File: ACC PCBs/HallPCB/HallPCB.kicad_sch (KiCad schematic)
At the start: 2 parts, among them J1 Conn_01x04_Socket, U1 TLE49643MXTMA1

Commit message: All boards should be finished. ACC otw, and an earlier version of the main board otw
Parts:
- added U2: AP2127N-1.0, Package_TO_SOT_SMD:SOT-23, symbol Regulator_Linear:AP2127N-1.0
- J1: footprint (none) -> Connector_PinHeader_2.54mm:PinHeader_1x04_P2.54mm_Horizontal
- U1: footprint PG-SOT23-3-15_INF -> TLE49643MXTMA1:PG-SOT23-3-15_INF
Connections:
- net MAIN: now also U2.2 (VO)
- net RAWSWPOWER: now also U2.3 (VI)
- net VOUT: now also U1.2 (Q); no longer U1.1 (VDD)
- new net SIG: U1.1 (VDD), U2.1 (GATE)
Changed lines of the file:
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@@
 	(global_label "VOUT"
 		(shape input)
+		(at 160.02 107.95 0)
+		(fields_autoplaced yes)
+		(effects
+			(font
+				(size 1.27 1.27)
+			)
+			(justify left)
+		)
+		(property "Intersheetrefs" "${INTERSHEET_REFS}"
+			(at 167.7224 107.95 0)
+			(effects
+				(font
+					(size 1.27 1.27)
+				)
+				(justify left)
+				(hide yes)
+			)
+		)
+	)
+	(global_label "RAWSWPOWER"
+		(shape input)
+		(at 142.24 86.36 180)
+		(fields_autoplaced yes)
+		(effects
+			(font
+				(size 1.27 1.27)
+			)
+			(justify right)
+		)
+		(property "Intersheetrefs" "${INTERSHEET_REFS}"
+			(at 126.313 86.36 0)
+			(effects
+				(font
+					(size 1.27 1.27)
+				)
+				(justify right)
+				(hide yes)
+			)
+		)
+	)
+	(global_label "MAIN"
+		(shape input)
+		(at 149.86 121.92 0)
+		(fields_autoplaced yes)
+		(effects
+			(font
+				(size 1.27 1.27)
+			)
+			(justify left)
+		)
+		(property "Intersheetrefs" "${INTERSHEET_REFS}"
+			(at 157.3205 121.92 0)
+			(effects
+				(font
+					(size 1.27 1.27)
+				)
+				(justify left)
+				(hide yes)
+			)
+		)
+	)
+	(global_label "RAWSWPOWER"
+		(shape input)
+		(at 134.62 121.92 180)
+		(fields_autoplaced yes)
+		(effects
+			(font
+				(size 1.27 1.27)
+			)
+			(justify right)
+		)
+		(property "Intersheetrefs" "${INTERSHEET_REFS}"
+			(at 118.693 121.92 0)
+			(effects
+				(font
+					(size 1.27 1.27)
+				)
+				(justify right)
+				(hide yes)
+			)
+		)
+	)
+	(global_label "MAIN"
+		(shape input)
+		(at 142.24 81.28 180)
+		(fields_autoplaced yes)
+		(effects
+			(font
+				(size 1.27 1.27)
+			)
+			(justify right)
+		)
+		(property "Intersheetrefs" "${INTERSHEET_REFS}"
+			(at 134.7795 81.28 0)
+			(effects
+				(font
+					(size 1.27 1.27)
+				)
+				(justify right)
+				(hide yes)
+			)
+		)
+	)
+	(global_label "VOUT"
+		(shape input)
+		(at 142.24 88.9 180)
+		(fields_autoplaced yes)
+		(effects
+			(font
+				(size 1.27 1.27)
+			)
+			(justify right)
+		)
+		(property "Intersheetrefs" "${INTERSHEET_REFS}"
+			(at 134.5376 88.9 0)
+			(effects
+				(font
+					(size 1.27 1.27)
+				)
+				(justify right)
+				(hide yes)
+			)
+		)
+	)
+	(global_label "GND"
+		(shape input)
+		(at 142.24 83.82 180)
+		(fields_autoplaced yes)
+		(effects
+			(font
+				(size 1.27 1.27)
+			)
+			(justify right)
+		)
+		(property "Intersheetrefs" "${INTERSHEET_REFS}"
+			(at 135.3843 83.82 0)
+			(effects
+				(font
+					(size 1.27 1.27)
+				)
+				(justify right)
+				(hide yes)
+			)
+		)
+	)
+	(global_label "GND"
+		(shape input)
+		(at 160.02 105.41 0)
+		(fields_autoplaced yes)
+		(effects
+			(font
+				(size 1.27 1.27)
+			)
+			(justify left)
+		)
+		(property "Intersheetrefs" "${INTERSHEET_REFS}"
+			(at 166.8757 105.41 0)
+			(effects
+				(font
+					(size 1.27 1.27)
+				)
+				(justify left)
+				(hide yes)
+			)
+		)
+	)
+	(global_label "SIG"
+		(shape input)
+		(at 142.24 129.54 270)
+		(fields_autoplaced yes)
+		(effects
+			(font
+				(size 1.27 1.27)
+			)
+			(justify right)
+		)
+		(property "Intersheetrefs" "${INTERSHEET_REFS}"
+			(at 142.24 135.6095 90)
+			(effects
+				(font
+					(size 1.27 1.27)
+				)
+				(justify right)
+				(hide yes)
+			)
+		)
+	)
+	(global_label "SIG"
+		(shape input)
 		(at 119.38 105.41 180)
 		(fields_autoplaced yes)
@@
 		)
 		(property "Intersheetrefs" "${INTERSHEET_REFS}"
-			(at 111.6776 105.41 0)
-			(effects
-				(font
-					(size 1.27 1.27)
-				)
-				(justify right)
-				(hide yes)
-			)
-		)
-	)
-	(global_label "RAWSWPOWER"
-		(shape input)
-		(at 142.24 86.36 180)
-		(fields_autoplaced yes)
-		(effects
-			(font
-				(size 1.27 1.27)
-			)
-			(justify right)
-		)
-		(property "Intersheetrefs" "${INTERSHEET_REFS}"
-			(at 126.313 86.36 0)
-			(effects
-				(font
-					(size 1.27 1.27)
-				)
-				(justify right)
-				(hide yes)
-			)
-		)
-	)
-	(global_label "MAIN"
-		(shape input)
-		(at 142.24 81.28 180)
-		(fields_autoplaced yes)
-		(effects
-			(font
-				(size 1.27 1.27)
-			)
-			(justify right)
-		)
-		(property "Intersheetrefs" "${INTERSHEET_REFS}"
-			(at 134.7795 81.28 0)
-			(effects
-				(font
-					(size 1.27 1.27)
-				)
-				(justify right)
-				(hide yes)
-			)
-		)
-	)
-	(global_label "VOUT"
-		(shape input)
-		(at 142.24 88.9 180)
-		(fields_autoplaced yes)
-		(effects
-			(font
-				(size 1.27 1.27)
-			)
-			(justify right)
-		)
-		(property "Intersheetrefs" "${INTERSHEET_REFS}"
-			(at 134.5376 88.9 0)
-			(effects
-				(font
-					(size 1.27 1.27)
-				)
-				(justify right)
-				(hide yes)
-			)
-		)
-	)
-	(global_label "GND"
-		(shape input)
-		(at 142.24 83.82 180)
-		(fields_autoplaced yes)
-		(effects
-			(font
-				(size 1.27 1.27)
-			)
-			(justify right)
-		)
-		(property "Intersheetrefs" "${INTERSHEET_REFS}"
-			(at 135.3843 83.82 0)
-			(effects
-				(font
-					(size 1.27 1.27)
-				)
-				(justify right)
-				(hide yes)
-			)
-		)
-	)
-	(global_label "GND"
-		(shape input)
-		(at 160.02 105.41 0)
-		(fields_autoplaced yes)
-		(effects
-			(font
-				(size 1.27 1.27)
-			)
-			(justify left)
-		)
-		(property "Intersheetrefs" "${INTERSHEET_REFS}"
-			(at 166.8757 105.41 0)
-			(effects
-				(font
-					(size 1.27 1.27)
-				)
-				(justify left)
-				(hide yes)
+			(at 113.3105 105.41 0)
+			(effects
+				(font
+					(size 1.27 1.27)
+				)
+				(justify right)
+				(hide yes)
+			)
+		)
+	)
+	(symbol
+		(lib_id "Regulator_Linear:AP2127N-1.0")
+		(at 142.24 121.92 0)
+		(unit 1)
+		(exclude_from_sim no)
+		(in_bom yes)
+		(on_board yes)
+		(dnp no)
+		(fields_autoplaced yes)
+		(property "Reference" "U2"
+			(at 142.24 115.57 0)
+			(effects
+				(font
+					(size 1.27 1.27)
+				)
+			)
+		)
+		(property "Value" "AP2127N-1.0"
+			(at 142.24 118.11 0)
+			(effects
+				(font
+					(size 1.27 1.27)
+				)
+			)
+		)
+		(property "Footprint" "Package_TO_SOT_SMD:SOT-23"
+			(at 142.24 116.205 0)
+			(effects
+				(font
+					(size 1.27 1.27)
+					(italic yes)
+				)
+				(hide yes)
+			)
+		)
+		(property "Datasheet" "https://www.diodes.com/assets/Datasheets/AP2127.pdf"
+			(at 142.24 121.92 0)
+			(effects
+				(font
+					(size 1.27 1.27)
+				)
+				(hide yes)
+			)
+		)
+		(property "Description" "300mA low dropout linear regulator, shutdown pin, 2.5V-6V input voltage, 1.0V fixed positive output, SOT-23 package"
+			(at 142.24 121.92 0)
+			(effects
+				(font
+					(size 1.27 1.27)
+				)
+				(hide yes)
+			)
+		)
+		(pin "3"
+		)
+		(pin "1"
+		)
+		(pin "2"
+		)
+		(instances
+			(project ""
+				(path "/bca63e1f-d422-43ee-b63a-c2b8269ab195"
+					(reference "U2")
+					(unit 1)
+				)
 			)
 		)
@@
 			)
 		)
-		(property "Footprint" "PG-SOT23-3-15_INF"
+		(property "Footprint" "TLE49643MXTMA1:PG-SOT23-3-15_INF"
 			(at 119.38 105.41 0)
 			(effects
@@
 			)
 		)
-		(property "Footprint" ""
+		(property "Footprint" "Connector_PinHeader_2.54mm:PinHeader_1x04_P2.54mm_Horizontal"
 			(at 147.32 83.82 0)
 			(effects

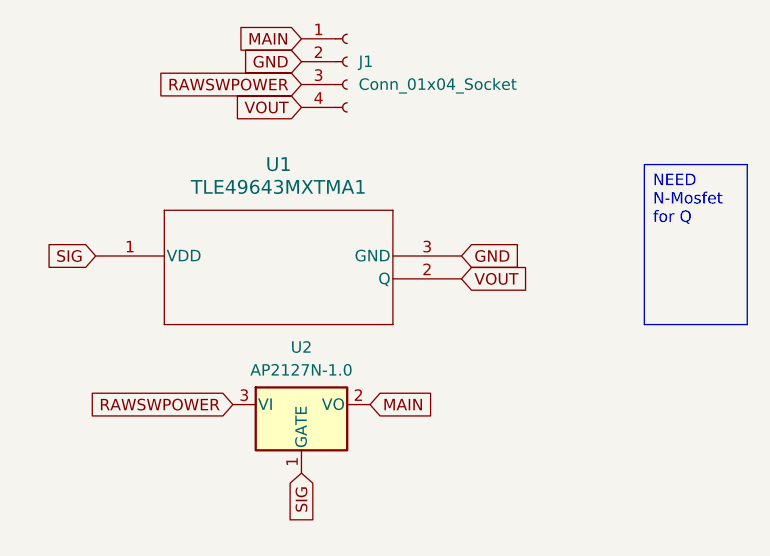
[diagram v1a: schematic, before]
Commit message: post R1 - flipped many traces and worked on adding an internal sensor for reduncancy
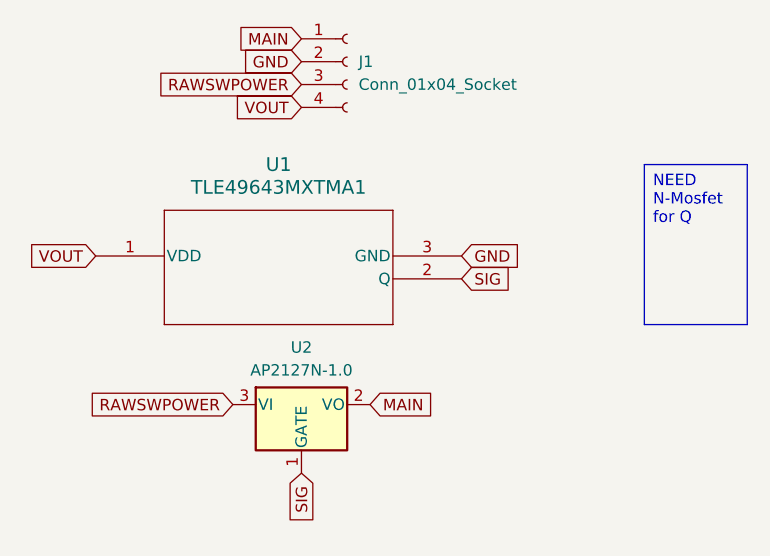
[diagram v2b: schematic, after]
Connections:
- net SIG: now also U1.2 (Q); no longer U1.1 (VDD)
- net VOUT: now also U1.1 (VDD); no longer U1.2 (Q)
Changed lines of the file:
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@@
 	(global_label "VOUT"
 		(shape input)
+		(at 119.38 105.41 180)
+		(fields_autoplaced yes)
+		(effects
+			(font
+				(size 1.27 1.27)
+			)
+			(justify right)
+		)
+		(property "Intersheetrefs" "${INTERSHEET_REFS}"
+			(at 111.6776 105.41 0)
+			(effects
+				(font
+					(size 1.27 1.27)
+				)
+				(justify right)
+				(hide yes)
+			)
+		)
+	)
+	(global_label "RAWSWPOWER"
+		(shape input)
+		(at 142.24 86.36 180)
+		(fields_autoplaced yes)
+		(effects
+			(font
+				(size 1.27 1.27)
+			)
+			(justify right)
+		)
+		(property "Intersheetrefs" "${INTERSHEET_REFS}"
+			(at 126.313 86.36 0)
+			(effects
+				(font
+					(size 1.27 1.27)
+				)
+				(justify right)
+				(hide yes)
+			)
+		)
+	)
+	(global_label "MAIN"
+		(shape input)
+		(at 149.86 121.92 0)
+		(fields_autoplaced yes)
+		(effects
+			(font
+				(size 1.27 1.27)
+			)
+			(justify left)
+		)
+		(property "Intersheetrefs" "${INTERSHEET_REFS}"
+			(at 157.3205 121.92 0)
+			(effects
+				(font
+					(size 1.27 1.27)
+				)
+				(justify left)
+				(hide yes)
+			)
+		)
+	)
+	(global_label "RAWSWPOWER"
+		(shape input)
+		(at 134.62 121.92 180)
+		(fields_autoplaced yes)
+		(effects
+			(font
+				(size 1.27 1.27)
+			)
+			(justify right)
+		)
+		(property "Intersheetrefs" "${INTERSHEET_REFS}"
+			(at 118.693 121.92 0)
+			(effects
+				(font
+					(size 1.27 1.27)
+				)
+				(justify right)
+				(hide yes)
+			)
+		)
+	)
+	(global_label "MAIN"
+		(shape input)
+		(at 142.24 81.28 180)
+		(fields_autoplaced yes)
+		(effects
+			(font
+				(size 1.27 1.27)
+			)
+			(justify right)
+		)
+		(property "Intersheetrefs" "${INTERSHEET_REFS}"
+			(at 134.7795 81.28 0)
+			(effects
+				(font
+					(size 1.27 1.27)
+				)
+				(justify right)
+				(hide yes)
+			)
+		)
+	)
+	(global_label "VOUT"
+		(shape input)
+		(at 142.24 88.9 180)
+		(fields_autoplaced yes)
+		(effects
+			(font
+				(size 1.27 1.27)
+			)
+			(justify right)
+		)
+		(property "Intersheetrefs" "${INTERSHEET_REFS}"
+			(at 134.5376 88.9 0)
+			(effects
+				(font
+					(size 1.27 1.27)
+				)
+				(justify right)
+				(hide yes)
+			)
+		)
+	)
+	(global_label "GND"
+		(shape input)
+		(at 142.24 83.82 180)
+		(fields_autoplaced yes)
+		(effects
+			(font
+				(size 1.27 1.27)
+			)
+			(justify right)
+		)
+		(property "Intersheetrefs" "${INTERSHEET_REFS}"
+			(at 135.3843 83.82 0)
+			(effects
+				(font
+					(size 1.27 1.27)
+				)
+				(justify right)
+				(hide yes)
+			)
+		)
+	)
+	(global_label "GND"
+		(shape input)
+		(at 160.02 105.41 0)
+		(fields_autoplaced yes)
+		(effects
+			(font
+				(size 1.27 1.27)
+			)
+			(justify left)
+		)
+		(property "Intersheetrefs" "${INTERSHEET_REFS}"
+			(at 166.8757 105.41 0)
+			(effects
+				(font
+					(size 1.27 1.27)
+				)
+				(justify left)
+				(hide yes)
+			)
+		)
+	)
+	(global_label "SIG"
+		(shape input)
+		(at 142.24 129.54 270)
+		(fields_autoplaced yes)
+		(effects
+			(font
+				(size 1.27 1.27)
+			)
+			(justify right)
+		)
+		(property "Intersheetrefs" "${INTERSHEET_REFS}"
+			(at 142.24 135.6095 90)
+			(effects
+				(font
+					(size 1.27 1.27)
+				)
+				(justify right)
+				(hide yes)
+			)
+		)
+	)
+	(global_label "SIG"
+		(shape input)
 		(at 160.02 107.95 0)
 		(fields_autoplaced yes)
@@
 		)
 		(property "Intersheetrefs" "${INTERSHEET_REFS}"
-			(at 167.7224 107.95 0)
+			(at 166.0895 107.95 0)
 			(effects
 				(font
@@
 				(hide yes)
 			)
-		)
-	)
-	(global_label "RAWSWPOWER"
-		(shape input)
-		(at 142.24 86.36 180)
-		(fields_autoplaced yes)
-		(effects
-			(font
-				(size 1.27 1.27)
-			)
-			(justify right)
-		)
-		(property "Intersheetrefs" "${INTERSHEET_REFS}"
-			(at 126.313 86.36 0)
-			(effects
-				(font
-					(size 1.27 1.27)
-				)
-				(justify right)
-				(hide yes)
-			)
-		)
-	)
-	(global_label "MAIN"
-		(shape input)
-		(at 149.86 121.92 0)
-		(fields_autoplaced yes)
-		(effects
-			(font
-				(size 1.27 1.27)
-			)
-			(justify left)
-		)
-		(property "Intersheetrefs" "${INTERSHEET_REFS}"
-			(at 157.3205 121.92 0)
-			(effects
-				(font
-					(size 1.27 1.27)
-				)
-				(justify left)
-				(hide yes)
-			)
-		)
-	)
-	(global_label "RAWSWPOWER"
-		(shape input)
-		(at 134.62 121.92 180)
-		(fields_autoplaced yes)
-		(effects
-			(font
-				(size 1.27 1.27)
-			)
-			(justify right)
-		)
-		(property "Intersheetrefs" "${INTERSHEET_REFS}"
-			(at 118.693 121.92 0)
-			(effects
-				(font
-					(size 1.27 1.27)
-				)
-				(justify right)
-				(hide yes)
-			)
-		)
-	)
-	(global_label "MAIN"
-		(shape input)
-		(at 142.24 81.28 180)
-		(fields_autoplaced yes)
-		(effects
-			(font
-				(size 1.27 1.27)
-			)
-			(justify right)
-		)
-		(property "Intersheetrefs" "${INTERSHEET_REFS}"
-			(at 134.7795 81.28 0)
-			(effects
-				(font
-					(size 1.27 1.27)
-				)
-				(justify right)
-				(hide yes)
-			)
-		)
-	)
-	(global_label "VOUT"
-		(shape input)
-		(at 142.24 88.9 180)
-		(fields_autoplaced yes)
-		(effects
-			(font
-				(size 1.27 1.27)
-			)
-			(justify right)
-		)
-		(property "Intersheetrefs" "${INTERSHEET_REFS}"
-			(at 134.5376 88.9 0)
-			(effects
-				(font
-					(size 1.27 1.27)
-				)
-				(justify right)
-				(hide yes)
-			)
-		)
-	)
-	(global_label "GND"
-		(shape input)
-		(at 142.24 83.82 180)
-		(fields_autoplaced yes)
-		(effects
-			(font
-				(size 1.27 1.27)
-			)
-			(justify right)
-		)
-		(property "Intersheetrefs" "${INTERSHEET_REFS}"
-			(at 135.3843 83.82 0)
-			(effects
-				(font
-					(size 1.27 1.27)
-				)
-				(justify right)
-				(hide yes)
-			)
-		)
-	)
-	(global_label "GND"
-		(shape input)
-		(at 160.02 105.41 0)
-		(fields_autoplaced yes)
-		(effects
-			(font
-				(size 1.27 1.27)
-			)
-			(justify left)
-		)
-		(property "Intersheetrefs" "${INTERSHEET_REFS}"
-			(at 166.8757 105.41 0)
-			(effects
-				(font
-					(size 1.27 1.27)
-				)
-				(justify left)
-				(hide yes)
-			)
-		)
-	)
-	(global_label "SIG"
-		(shape input)
-		(at 142.24 129.54 270)
-		(fields_autoplaced yes)
-		(effects
-			(font
-				(size 1.27 1.27)
-			)
-			(justify right)
-		)
-		(property "Intersheetrefs" "${INTERSHEET_REFS}"
-			(at 142.24 135.6095 90)
-			(effects
-				(font
-					(size 1.27 1.27)
-				)
-				(justify right)
-				(hide yes)
-			)
-		)
-	)
-	(global_label "SIG"
-		(shape input)
-		(at 119.38 105.41 180)
-		(fields_autoplaced yes)
-		(effects
-			(font
-				(size 1.27 1.27)
-			)
-			(justify right)
-		)
-		(property "Intersheetrefs" "${INTERSHEET_REFS}"
-			(at 113.3105 105.41 0)
-			(effects
-				(font
-					(size 1.27 1.27)
-				)
-				(justify right)
-				(hide yes)
-			)
